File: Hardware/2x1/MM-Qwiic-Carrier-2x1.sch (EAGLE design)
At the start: 53 parts, among them J15 MICROMOD-2222-C, J2 QWIIC_RIGHT_ANGLE, U1 MCP73831, U5 AP7361C-33FGEUDFN-8

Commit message: Fix silk screen
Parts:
- removed H10, H11, H12, H13, H6, H7, H8, H9: STAND-OFF-REFLOW2.5MM_TALL, SparkFun-Hardware:STAND-OFF-REFLOW2.5MM_TALL
- removed JP1: JUMPER-SMT_2_NC_TRACE_SILK, SparkFun-Jumpers:JUMPER-SMT_2_NC_TRACE_SILK
- added D5: 3A/10V/280mV, SparkFun-DiscreteSemi:DIODE-SCHOTTKY-BAT60A
- added J4: (no value), SparkFun-Connectors:CONN_021X02_NO_SILK
- added J5: Vertical Qwiic Connector, SparkFun-Connectors:QWIIC_CONNECTOR
- added J6: (no value), SparkFun-Connectors:CONN_08NO_SILK_FEMALE_PTH
- added TP1, TP2: TEST-POINT3X5, SparkFun-Connectors:TEST-POINT3X5
- added U$32, U$5: QWIIC_BOARD_OUTLINESTANDOFF, SparkFun-Boards:QWIIC_BOARD_OUTLINESTANDOFF
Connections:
- removed net 5V: C4.1, D3.C, D4.A, JP1.2, U1.VIN
- removed net I2C_SCL: J15.I2C_SCL, J2.4
- removed net I2C_SDA: J15.I2C_SDA, J2.3
- removed net N$5: C3.1, D3.A, J3.+, U1.VBAT
- new net D0: J15.D0, J6.3
- new net D1: J15.D1/CAM_TRIG, J6.4
- new net I2C_!INT!: J15.I2C_!INT!, J6.2
- new net SCL: J15.I2C_SCL, J2.4, J5.4, TP2.1
- new net SDA: J15.I2C_SDA, J2.3, J5.3, TP1.1
- new net SPI_!CS!: J15.SPI_!CS!, J6.8
- new net SPI_CIPO: J15.SPI_SDI, J6.5
- new net SPI_COPI: J15.SPI_SDO, J6.6
- new net SPI_SCK: J15.SPI_SCK, J6.7
- new net V_BATT: C3.1, D3.A, J3.+, J4.1, U1.VBAT
- net 3.3V: now also J5.2
- net GND: now also J4.2, J5.1, J6.1; no longer H10.1, H11.1, H12.1, H13.1, H6.1, H7.1, H8.1, H9.1
- net N$3: now also D4.C; no longer U1.STAT
- net N$8: now also U1.STAT; no longer D4.C
- net VIN: now also D3.C, D5.C; no longer JP1.1
- net V_USB: now also C4.1, D4.A, D5.A, U1.VIN
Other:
- note added: "Cut this jumper and use the PTH holes to measure current draw"
- note added: "Cut this jumper to remove power LED."
- note added: "Header"
- note added: "Power Source Select"
- note added: "Qwiic Stand offs"
- note added: "Qwiic bus conservative max current: 226mA"
- note added: "Test Points"
- note removed: "Cut these jumpers to remove power LEDs."
- note removed: "Stand offs"
- moved on the sheet: C3, C4, D3, D4, J2, J3, R1, R4, R5, S1, S2, U1

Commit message: silkscreen
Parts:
- renumbered U$32 to U$34
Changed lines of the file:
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@@
 <part name="GND26" library="SparkFun-PowerSymbols" deviceset="GND" device=""/>
 <part name="U$5" library="SparkFun-Boards" deviceset="QWIIC_BOARD_OUTLINE" device="STANDOFF"/>
-<part name="U$32" library="SparkFun-Boards" deviceset="QWIIC_BOARD_OUTLINE" device="STANDOFF"/>
+<part name="U$34" library="SparkFun-Boards" deviceset="QWIIC_BOARD_OUTLINE" device="STANDOFF"/>
 </parts>
 <sheets>
@@
 <text x="299.974" y="271.526" size="2.54" layer="94" font="vector" align="center">Voltage Regulation</text>
 <text x="320.04" y="254" size="1.778" layer="97" font="vector">Range: 2.2 - 6.0V</text>
-<text x="261.62" y="218.44" size="1.778" layer="97">Close this jumper to
+<text x="261.62" y="218.44" size="1.778" layer="97" font="vector">Close this jumper to
 control the VREG in
 super low-power modes</text>
@@
 <wire x1="330.2" y1="193.04" x2="431.8" y2="193.04" width="0.2032" layer="97" style="longdash"/>
 <wire x1="431.8" y1="193.04" x2="431.8" y2="195.58" width="0.2032" layer="97" style="longdash"/>
-<text x="121.92" y="104.14" size="2.54" layer="94" align="center">Qwiic Connector</text>
-<text x="210.82" y="104.14" size="2.54" layer="94" align="center">Buttons</text>
-<text x="259.08" y="180.34" size="2.54" layer="94" align="center">Battery Charger</text>
-<text x="289.56" y="106.68" size="2.54" layer="94" align="center">Qwiic Stand offs</text>
+<text x="121.92" y="104.14" size="2.54" layer="94" font="vector" align="center">Qwiic Connector</text>
+<text x="210.82" y="104.14" size="2.54" layer="94" font="vector" align="center">Buttons</text>
+<text x="259.08" y="180.34" size="2.54" layer="94" font="vector" align="center">Battery Charger</text>
+<text x="289.56" y="106.68" size="2.54" layer="94" font="vector" align="center">Qwiic Stand offs</text>
 <wire x1="254" y1="111.76" x2="330.2" y2="111.76" width="0.2032" layer="97" style="longdash"/>
 <wire x1="330.2" y1="111.76" x2="330.2" y2="38.1" width="0.2032" layer="97" style="longdash"/>
@@
 <wire x1="330.2" y1="132.08" x2="330.2" y2="193.04" width="0.2032" layer="97" style="longdash"/>
 <wire x1="330.2" y1="132.08" x2="431.8" y2="132.08" width="0.2032" layer="97" style="longdash"/>
-<text x="381" y="182.88" size="2.54" layer="94" align="center">Power Source Select</text>
-<text x="381" y="121.92" size="2.54" layer="94" align="center">Test Points</text>
+<text x="381" y="182.88" size="2.54" layer="94" font="vector" align="center">Power Source Select</text>
+<text x="381" y="121.92" size="2.54" layer="94" font="vector" align="center">Test Points</text>
 <text x="111.76" y="25.4" size="1.778" layer="97" font="vector">Qwiic bus conservative
 max current: 226mA</text>
 <wire x1="170.18" y1="58.42" x2="251.46" y2="58.42" width="0.2032" layer="97" style="longdash"/>
-<text x="208.28" y="50.8" size="2.54" layer="94" align="center">Header</text>
+<text x="208.28" y="50.8" size="2.54" layer="94" font="vector" align="center">Header</text>
 <text x="368.3" y="236.22" size="1.778" layer="97" font="vector">Cut this jumper and use the PTH
 holes to measure current draw</text>
@@
 </instance>
 <instance part="U$5" gate="G$1" x="289.56" y="60.96" smashed="yes"/>
-<instance part="U$32" gate="G$1" x="289.56" y="40.64" smashed="yes"/>
+<instance part="U$34" gate="G$1" x="289.56" y="40.64" smashed="yes"/>
 </instances>
 <busses>

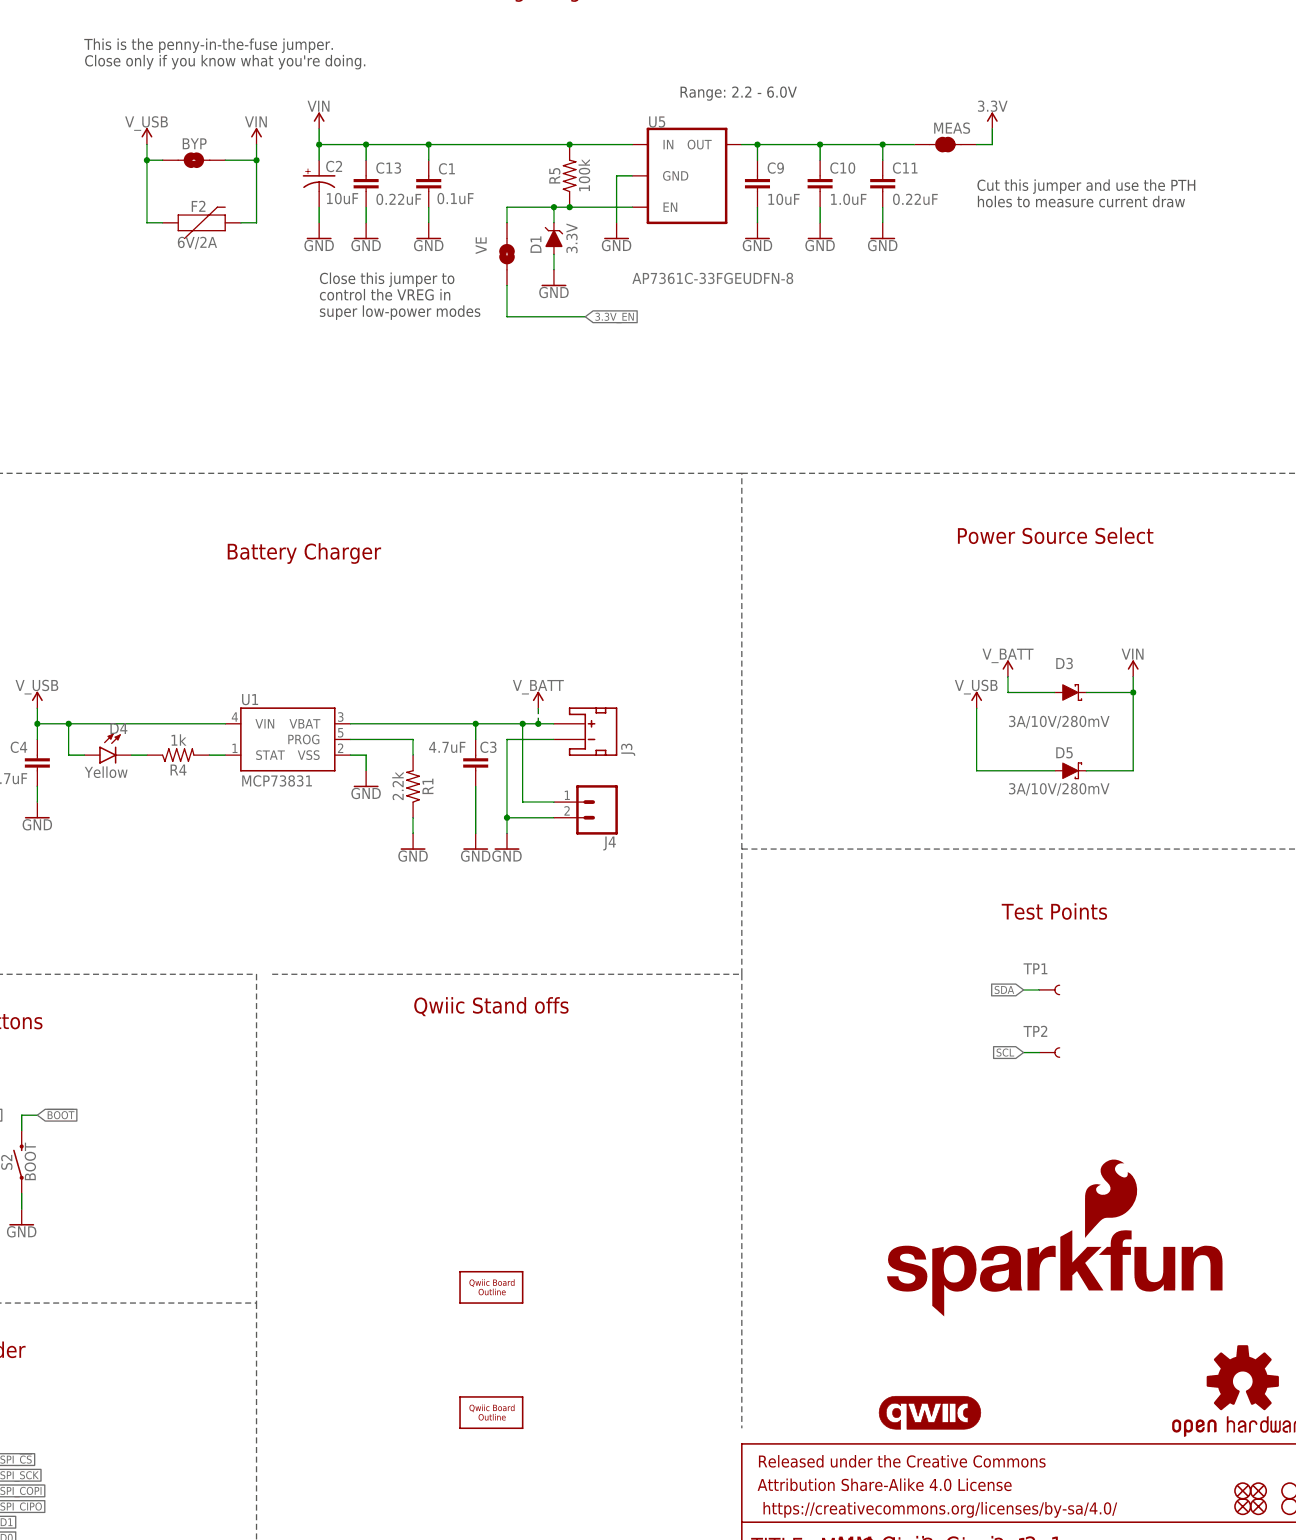
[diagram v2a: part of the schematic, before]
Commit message: silk screen
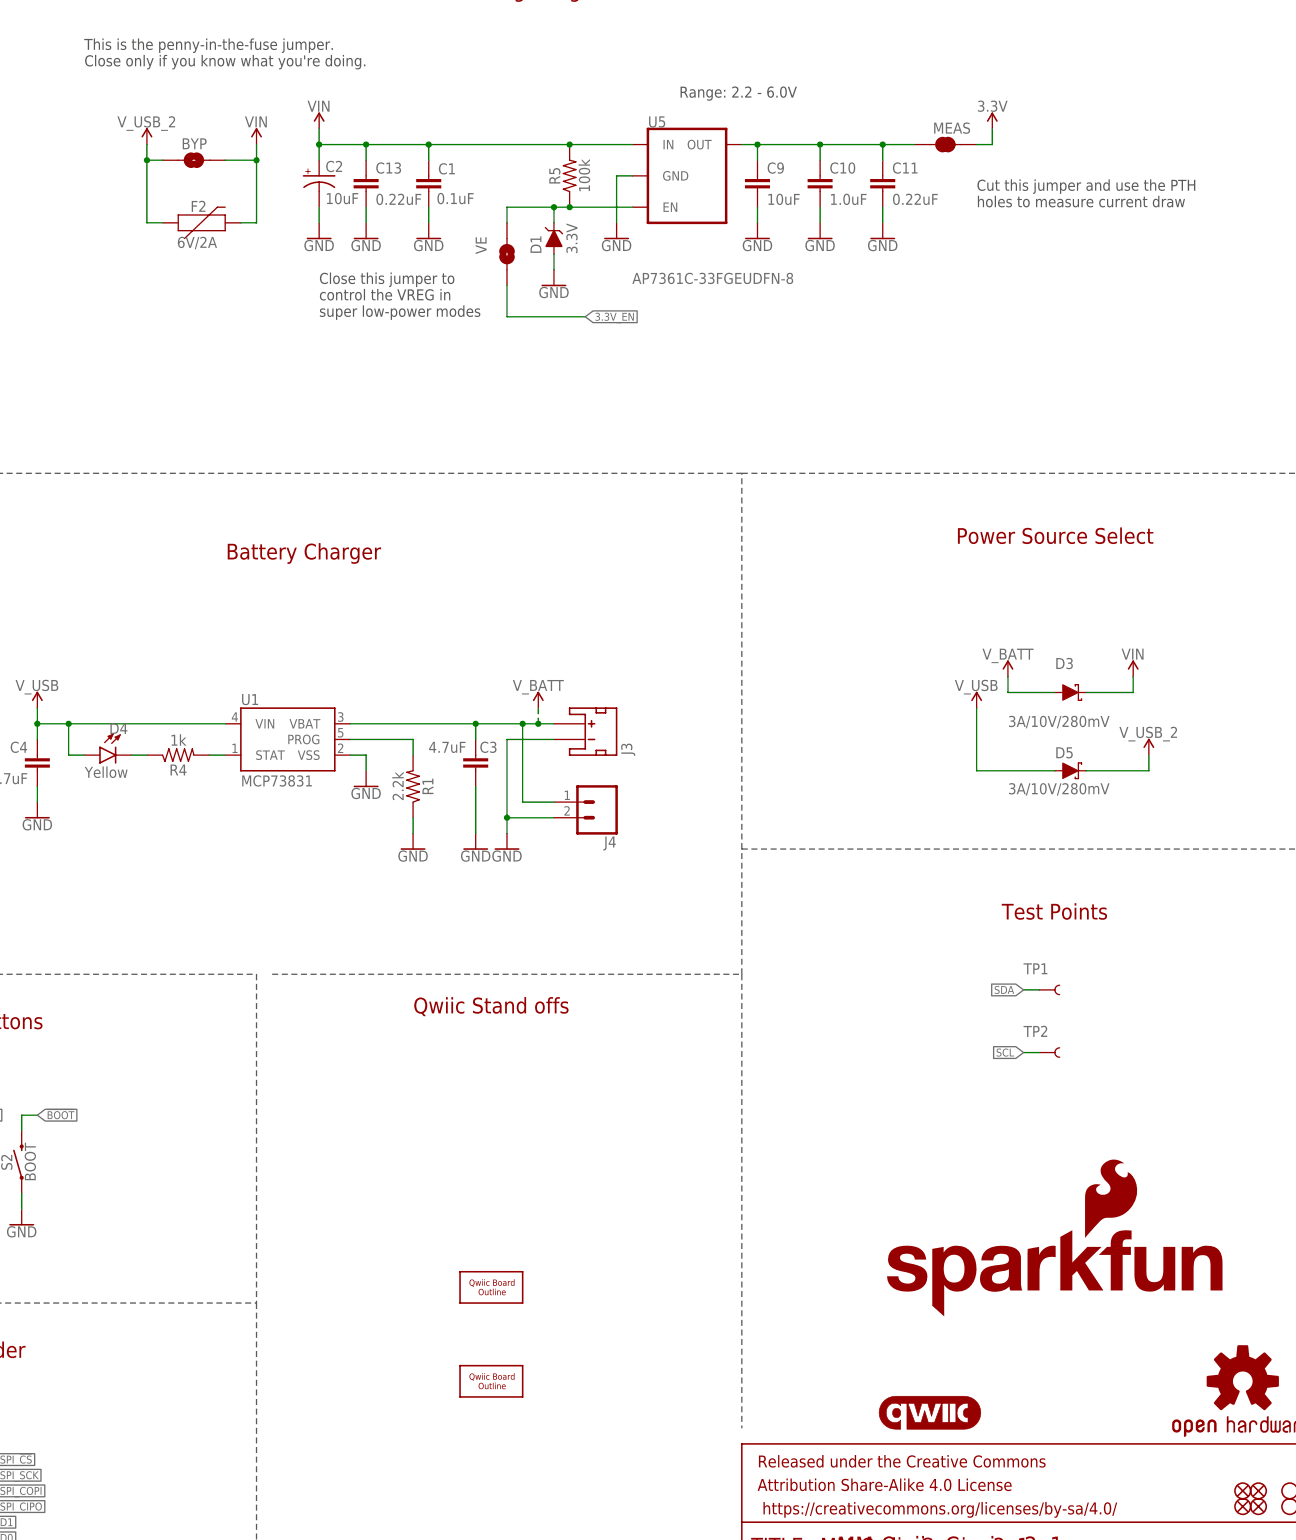
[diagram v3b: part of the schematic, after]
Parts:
- removed U$34: QWIIC_BOARD_OUTLINESTANDOFF, SparkFun-Boards:QWIIC_BOARD_OUTLINESTANDOFF
- added U$30: QWIIC_BOARD_OUTLINESTANDOFF, SparkFun-Boards:QWIIC_BOARD_OUTLINESTANDOFF
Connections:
- new net V_USB_2: BYP.1, D5.C, F2.1
- net VIN: no longer D5.C
- net V_USB: no longer BYP.1, F2.1
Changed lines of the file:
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@@
 <part name="BYP" library="SparkFun-Jumpers" deviceset="JUMPER-SMT_2_NO" device="_SILK" package3d_urn="urn:adsk.eagle:package:39279/1" value="JUMPER-SMT_2_NO_SILK"/>
 <part name="F2" library="SparkFun-Fuses" deviceset="PPTC" device="_6V2A" value="6V/2A"/>
-<part name="SUPPLY16" library="SparkFun-PowerSymbols" deviceset="V_USB" device=""/>
 <part name="U1" library="SparkFun-IC-Power" deviceset="MCP73831" device=""/>
 <part name="R1" library="SparkFun-Resistors" deviceset="2.2KOHM" device="-0603-1/10W-1%" value="2.2k"/>
@@
 <part name="GND26" library="SparkFun-PowerSymbols" deviceset="GND" device=""/>
 <part name="U$5" library="SparkFun-Boards" deviceset="QWIIC_BOARD_OUTLINE" device="STANDOFF"/>
-<part name="U$34" library="SparkFun-Boards" deviceset="QWIIC_BOARD_OUTLINE" device="STANDOFF"/>
+<part name="SUPPLY15" library="SparkFun-PowerSymbols" deviceset="V_USB_2" device=""/>
+<part name="SUPPLY16" library="SparkFun-PowerSymbols" deviceset="V_USB_2" device=""/>
+<part name="U$30" library="SparkFun-Boards" deviceset="QWIIC_BOARD_OUTLINE" device="STANDOFF"/>
 </parts>
 <sheets>
@@
 <attribute name="VALUE" x="241.808" y="231.394" size="1.778" layer="96" font="vector" align="top-center"/>
 </instance>
-<instance part="SUPPLY16" gate="G$1" x="233.68" y="246.38" smashed="yes">
-<attribute name="VALUE" x="233.68" y="249.174" size="1.778" layer="96" align="bottom-center"/>
-</instance>
 <instance part="U1" gate="G$1" x="256.54" y="149.86" smashed="yes">
 <attribute name="NAME" x="248.92" y="155.448" size="1.778" layer="95"/>
@@
 </instance>
 <instance part="U$5" gate="G$1" x="289.56" y="60.96" smashed="yes"/>
-<instance part="U$34" gate="G$1" x="289.56" y="40.64" smashed="yes"/>
+<instance part="SUPPLY15" gate="G$1" x="396.24" y="147.32" smashed="yes">
+<attribute name="VALUE" x="396.24" y="150.114" size="1.778" layer="96" align="bottom-center"/>
+</instance>
+<instance part="SUPPLY16" gate="G$1" x="233.68" y="246.38" smashed="yes">
+<attribute name="VALUE" x="233.68" y="249.174" size="1.778" layer="96" align="bottom-center"/>
+</instance>
+<instance part="U$30" gate="G$1" x="289.56" y="45.72" smashed="yes"/>
 </instances>
 <busses>
@@
 <wire x1="40.64" y1="66.04" x2="40.64" y2="68.58" width="0.1524" layer="91"/>
 <pinref part="SUPPLY5" gate="G$1" pin="V_USB"/>
-</segment>
-<segment>
-<wire x1="233.68" y1="233.68" x2="236.22" y2="233.68" width="0.1524" layer="91"/>
-<pinref part="BYP" gate="G$1" pin="1"/>
-<wire x1="236.22" y1="243.84" x2="233.68" y2="243.84" width="0.1524" layer="91"/>
-<wire x1="233.68" y1="243.84" x2="233.68" y2="233.68" width="0.1524" layer="91"/>
-<pinref part="F2" gate="F1" pin="1"/>
-<pinref part="SUPPLY16" gate="G$1" pin="V_USB"/>
-<wire x1="233.68" y1="246.38" x2="233.68" y2="243.84" width="0.1524" layer="91"/>
-<junction x="233.68" y="243.84"/>
 </segment>
 <segment>
@@
 <pinref part="D3" gate="G$1" pin="C"/>
 <wire x1="386.08" y1="157.48" x2="393.7" y2="157.48" width="0.1524" layer="91"/>
-<wire x1="393.7" y1="157.48" x2="393.7" y2="144.78" width="0.1524" layer="91"/>
-<pinref part="D5" gate="G$1" pin="C"/>
-<wire x1="393.7" y1="144.78" x2="386.08" y2="144.78" width="0.1524" layer="91"/>
 <wire x1="393.7" y1="157.48" x2="393.7" y2="160.02" width="0.1524" layer="91"/>
-<junction x="393.7" y="157.48"/>
 <pinref part="SUPPLY10" gate="G$1" pin="VIN"/>
 </segment>
@@
 </segment>
 </net>
+<net name="V_USB_2" class="0">
+<segment>
+<wire x1="233.68" y1="233.68" x2="236.22" y2="233.68" width="0.1524" layer="91"/>
+<pinref part="BYP" gate="G$1" pin="1"/>
+<wire x1="236.22" y1="243.84" x2="233.68" y2="243.84" width="0.1524" layer="91"/>
+<wire x1="233.68" y1="243.84" x2="233.68" y2="233.68" width="0.1524" layer="91"/>
+<pinref part="F2" gate="F1" pin="1"/>
+<pinref part="SUPPLY16" gate="G$1" pin="V_USB_2"/>
+<wire x1="233.68" y1="243.84" x2="233.68" y2="246.38" width="0.1524" layer="91"/>
+<junction x="233.68" y="243.84"/>
+</segment>
+<segment>
+<pinref part="D5" gate="G$1" pin="C"/>
+<wire x1="396.24" y1="144.78" x2="386.08" y2="144.78" width="0.1524" layer="91"/>
+<pinref part="SUPPLY15" gate="G$1" pin="V_USB_2"/>
+<wire x1="396.24" y1="144.78" x2="396.24" y2="147.32" width="0.1524" layer="91"/>
+</segment>
+</net>
